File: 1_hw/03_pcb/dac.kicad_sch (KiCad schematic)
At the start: 6 parts, among them U7 AD9744

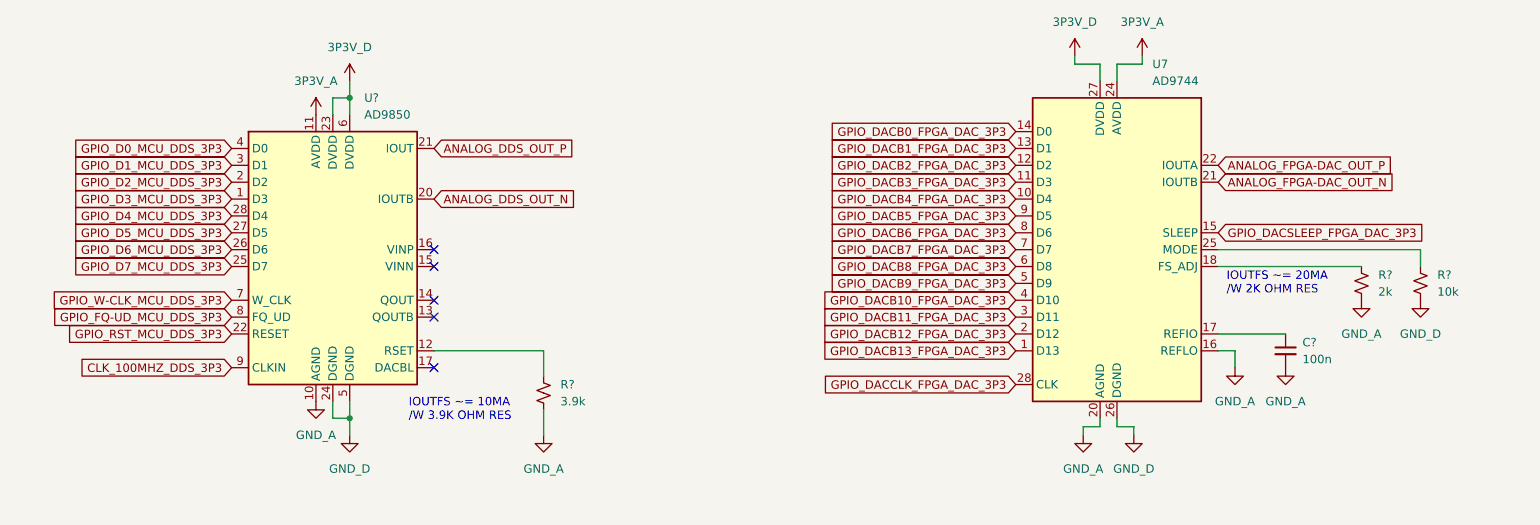
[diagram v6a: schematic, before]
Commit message: FEAT: Changed from two grounds (Digital + Analog) to Singular Ground IAW recommended Grounding Scheme.
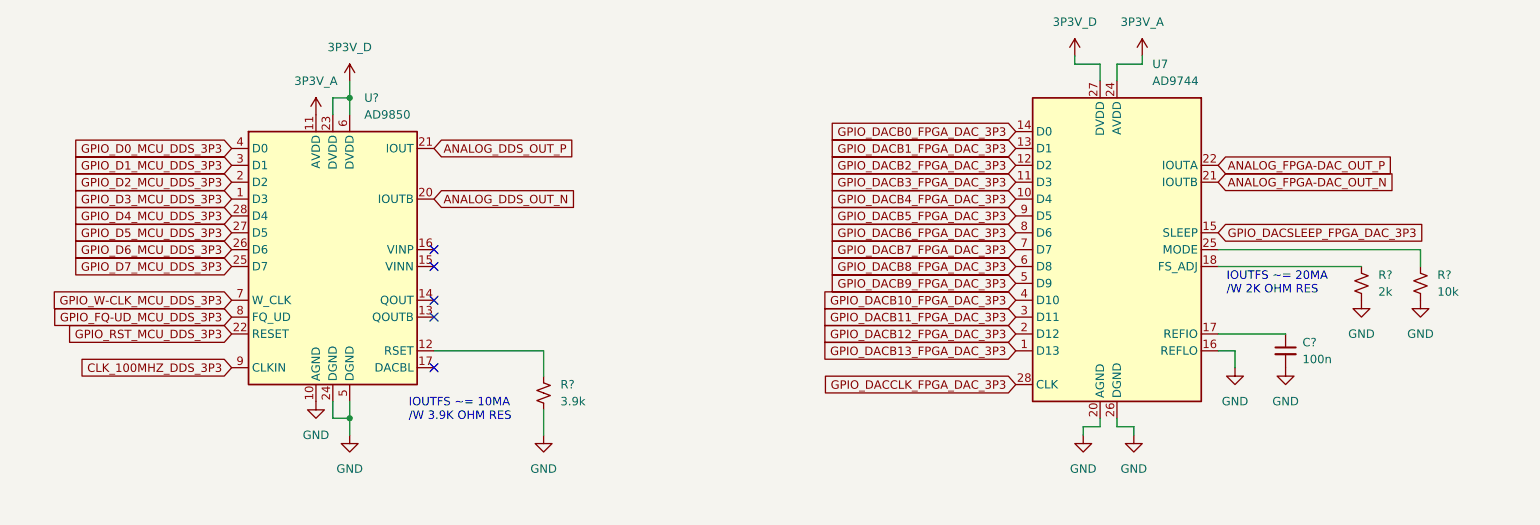
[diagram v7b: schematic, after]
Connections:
- net GND_D is gone; now on net GND: R?.2, U7.26 (DGND), U?.24 (DGND), U?.5 (DGND)
- net GND_A renamed GND
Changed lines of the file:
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@@
 			)
 		)
-		(property "Value" "GND_A"
+		(property "Value" "GND"
 			(at 204.47 119.38 0)
 			(effects
@@
 			)
 		)
-		(property "Value" "GND_A"
+		(property "Value" "GND"
 			(at 234.95 109.22 0)
 			(effects
@@
 			)
 		)
-		(property "Value" "GND_D"
+		(property "Value" "GND"
 			(at 212.09 119.38 0)
 			(effects
@@
 			)
 		)
-		(property "Value" "GND_A"
+		(property "Value" "GND"
 			(at 123.19 119.38 0)
 			(effects
@@
 			)
 		)
-		(property "Value" "GND_D"
+		(property "Value" "GND"
 			(at 93.98 119.38 0)
 			(effects
@@
 			)
 		)
-		(property "Value" "GND_D"
+		(property "Value" "GND"
 			(at 255.27 99.06 0)
 			(effects
@@
 			)
 		)
-		(property "Value" "GND_A"
+		(property "Value" "GND"
 			(at 246.38 99.06 0)
 			(effects
@@
 			)
 		)
-		(property "Value" "GND_A"
+		(property "Value" "GND"
 			(at 88.9 114.3 0)
 			(effects
@@
 			)
 		)
-		(property "Value" "GND_A"
+		(property "Value" "GND"
 			(at 227.33 109.22 0)
 			(effects

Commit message: FEAT: Added +15V and -15V Regulator. Replaced some Symbols to add additional Part Number Field.
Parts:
- U7: Part Number (none) -> AD9744ARUZRL7
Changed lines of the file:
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@@
+			)
+		)
+		(property "Part Number" "AD9744ARUZRL7"
+			(at 209.55 86.36 0)
+			(effects
+				(font
+					(size 1.27 1.27)
+				)
+				(hide yes)
 			)
 		)
